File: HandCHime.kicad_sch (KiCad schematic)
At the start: 18 parts, among them J1 USB_C_Receptacle_USB2.0, J2 Pins, SW0 BOOT, SW1 Row 0, Col 0, SW2 Row 0, Col 1, U1 CH552T, U2 USBLC6-2P6

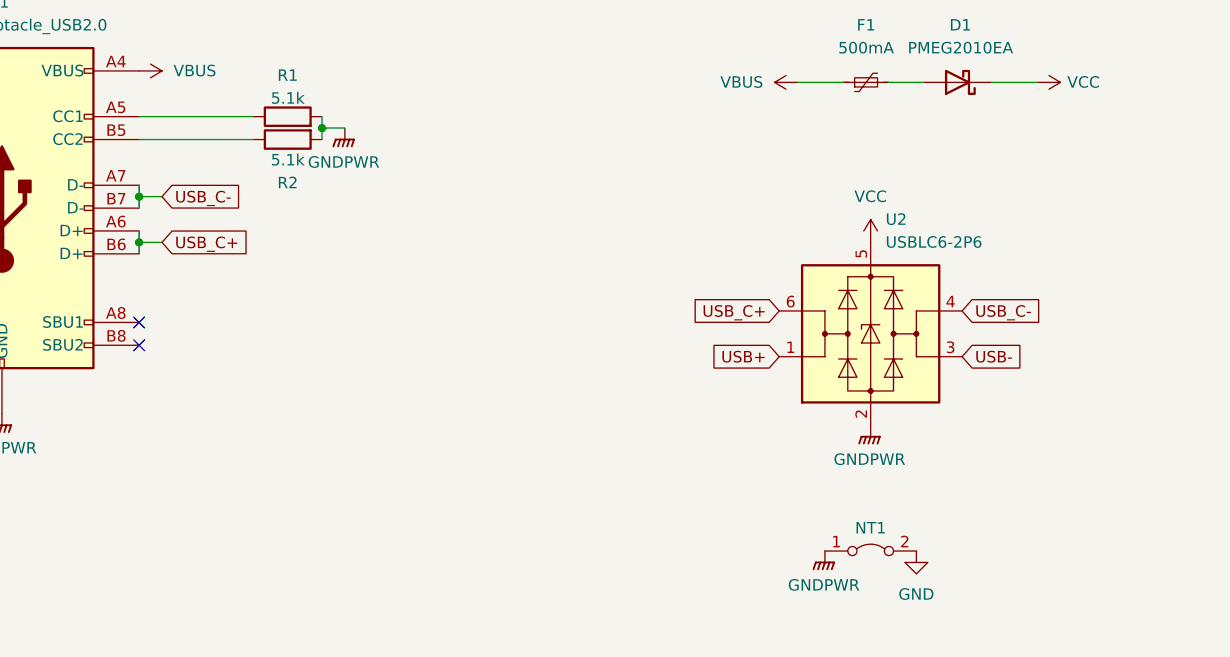
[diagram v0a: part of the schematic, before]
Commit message: Use smaller ESD chip
USBLC6-2SC6 → PRTR5V0U2X
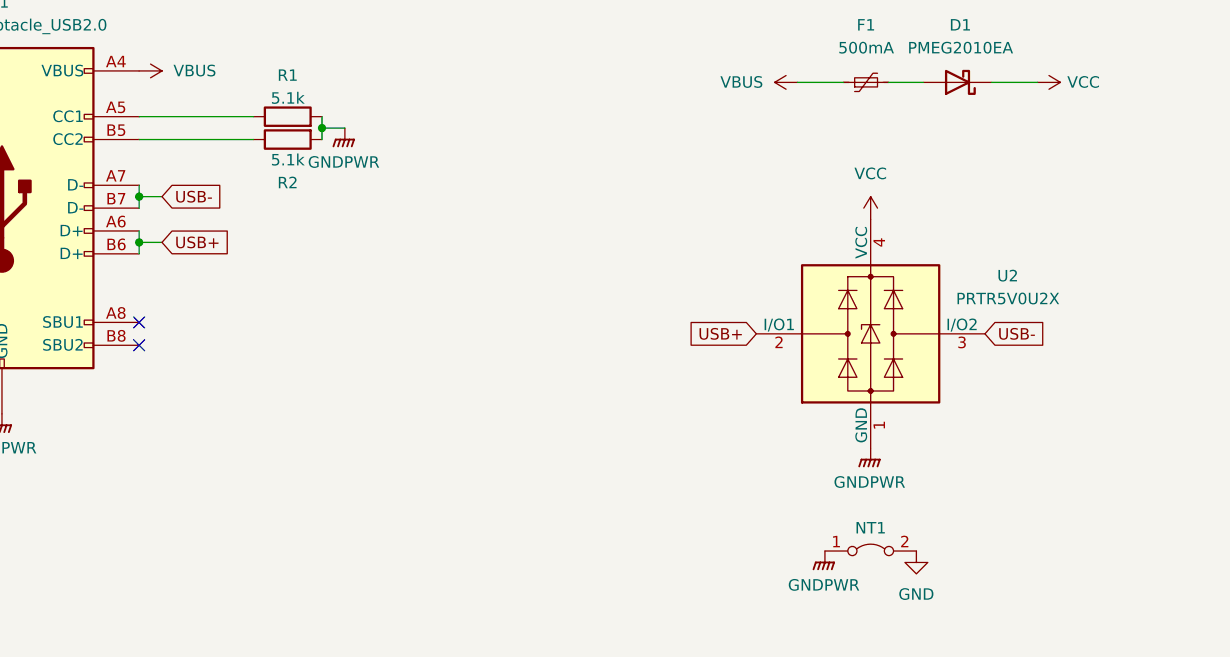
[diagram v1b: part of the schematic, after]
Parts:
- removed U2: USBLC6-2P6, Package_TO_SOT_SMD:SOT-23-6, symbol Power_Protection:USBLC6-2SC6
- added U2: PRTR5V0U2X, Package_TO_SOT_SMD:SOT-143, symbol Power_Protection:PRTR5V0U2X
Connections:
- net USB_C+ is gone; now on net USB+: J1.A6 (D+), J1.B6 (D+)
- net USB_C- is gone; now on net USB-: J1.A7 (D-), J1.B7 (D-)
- net GNDPWR: now also U2.1 (GND)
- net USB+: now also U2.2 (I/O1)
- net USB-: now also U2.3 (I/O2)
- net VCC: now also U2.4 (VCC)
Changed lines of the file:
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@@
 		)
 	)
-	(global_label "USB_C-"
-		(shape input)
-		(at 137.16 66.04 0)
-		(fields_autoplaced yes)
-		(effects
-			(font
-				(size 1.27 1.27)
-			)
-			(justify left)
-		)
-		(property "Intersheetrefs" "${INTERSHEET_REFS}"
-			(at 147.7652 66.04 0)
-			(effects
-				(font
-					(size 1.27 1.27)
-				)
-				(justify left)
-				(hide yes)
-			)
-		)
-	)
 	(global_label "P14"
 		(shape input)
@@
 		)
 	)
-	(global_label "USB_C+"
+	(global_label "USB+"
 		(shape input)
 		(at 48.26 58.42 0)
@@
 		)
 		(property "Intersheetrefs" "${INTERSHEET_REFS}"
-			(at 58.8652 58.42 0)
+			(at 56.6276 58.42 0)
 			(effects
 				(font
@@
 		)
 	)
-	(global_label "USB_C+"
-		(shape input)
-		(at 116.84 66.04 180)
-		(fields_autoplaced yes)
-		(effects
-			(font
-				(size 1.27 1.27)
-			)
-			(justify right)
-		)
-		(property "Intersheetrefs" "${INTERSHEET_REFS}"
-			(at 106.2348 66.04 0)
-			(effects
-				(font
-					(size 1.27 1.27)
-				)
-				(justify right)
-				(hide yes)
-			)
-		)
-	)
 	(global_label "USB-"
 		(shape input)
-		(at 137.16 71.12 0)
+		(at 139.7 68.58 0)
 		(fields_autoplaced yes)
 		(effects
@@
 		)
 		(property "Intersheetrefs" "${INTERSHEET_REFS}"
-			(at 145.5276 71.12 0)
+			(at 148.0676 68.58 0)
 			(effects
 				(font
@@
 		)
 	)
-	(global_label "USB_C-"
+	(global_label "USB-"
 		(shape input)
 		(at 48.26 53.34 0)
@@
 		)
 		(property "Intersheetrefs" "${INTERSHEET_REFS}"
-			(at 58.8652 53.34 0)
+			(at 56.6276 53.34 0)
 			(effects
 				(font
@@
 	(global_label "USB+"
 		(shape input)
-		(at 116.84 71.12 180)
+		(at 114.3 68.58 180)
 		(fields_autoplaced yes)
 		(effects
@@
 		)
 		(property "Intersheetrefs" "${INTERSHEET_REFS}"
-			(at 108.4724 71.12 0)
+			(at 105.9324 68.58 0)
 			(effects
 				(font
@@
 	)
 	(symbol
+		(lib_id "Power_Protection:PRTR5V0U2X")
+		(at 127 68.58 0)
+		(unit 1)
+		(exclude_from_sim no)
+		(in_bom yes)
+		(on_board yes)
+		(dnp no)
+		(fields_autoplaced yes)
+		(property "Reference" "U2"
+			(at 142.24 62.1598 0)
+			(effects
+				(font
+					(size 1.27 1.27)
+				)
+			)
+		)
+		(property "Value" "PRTR5V0U2X"
+			(at 142.24 64.6998 0)
+			(effects
+				(font
+					(size 1.27 1.27)
+				)
+			)
+		)
+		(property "Footprint" "Package_TO_SOT_SMD:SOT-143"
+			(at 128.524 68.58 0)
+			(effects
+				(font
+					(size 1.27 1.27)
+				)
+				(hide yes)
+			)
+		)
+		(property "Datasheet" "https://assets.nexperia.com/documents/data-sheet/PRTR5V0U2X.pdf"
+			(at 128.524 68.58 0)
+			(effects
+				(font
+					(size 1.27 1.27)
+				)
+				(hide yes)
+			)
+		)
+		(property "Description" "Ultra low capacitance double rail-to-rail ESD protection diode, SOT-143"
+			(at 127 68.58 0)
+			(effects
+				(font
+					(size 1.27 1.27)
+				)
+				(hide yes)
+			)
+		)
+		(property "LCSC" "C12333"
+			(at 127 68.58 0)
+			(effects
+				(font
+					(size 1.27 1.27)
+				)
+				(hide yes)
+			)
+		)
+		(property "DigiKey" "1727-3884-1-ND"
+			(at 127 68.58 0)
+			(effects
+				(font
+					(size 1.27 1.27)
+				)
+				(hide yes)
+			)
+		)
+		(pin "2"
+		)
+		(pin "3"
+		)
+		(pin "1"
+		)
+		(pin "4"
+		)
+		(instances
+			(project ""
+				(path "/34400e51-cf83-464a-b3ec-e9a28a972a27"
+					(reference "U2")
+					(unit 1)
+				)
+			)
+		)
+	)
+	(symbol
 		(lib_id "power:VCC")
-		(at 127 58.42 0)
+		(at 127 55.88 0)
 		(unit 1)
 		(exclude_from_sim no)
@@
 		(fields_autoplaced yes)
 		(property "Reference" "#PWR07"
-			(at 127 62.23 0)
+			(at 127 59.69 0)
 			(effects
 				(font
@@
 		)
 		(property "Value" "VCC"
-			(at 127 53.34 0)
+			(at 127 50.8 0)
 			(effects
 				(font
@@
 		)
 		(property "Footprint" ""
-			(at 127 58.42 0)
+			(at 127 55.88 0)
 			(effects
 				(font
@@
 		)
 		(property "Datasheet" ""
-			(at 127 58.42 0)
+			(at 127 55.88 0)
 			(effects
 				(font
@@
 		)
 		(property "Description" ""
-			(at 127 58.42 0)
+			(at 127 55.88 0)
 			(effects
 				(font
@@
 	)
 	(symbol
-		(lib_id "Power_Protection:USBLC6-2SC6")
-		(at 127 68.58 0)
-		(unit 1)
-		(exclude_from_sim no)
-		(in_bom yes)
-		(on_board yes)
-		(dnp no)
-		(fields_autoplaced yes)
-		(property "Reference" "U2"
-			(at 128.6511 55.88 0)
-			(effects
-				(font
-					(size 1.27 1.27)
-				)
-				(justify left)
-			)
-		)
-		(property "Value" "USBLC6-2P6"
-			(at 128.6511 58.42 0)
-			(effects
-				(font
-					(size 1.27 1.27)
-				)
-				(justify left)
-			)
-		)
-		(property "Footprint" "Package_TO_SOT_SMD:SOT-23-6"
-			(at 127 81.28 0)
-			(effects
-				(font
-					(size 1.27 1.27)
-				)
-				(hide yes)
-			)
-		)
-		(property "Datasheet" "https://www.st.com/resource/en/datasheet/usblc6-2.pdf"
-			(at 132.08 59.69 0)
-			(effects
-				(font
-					(size 1.27 1.27)
-				)
-				(hide yes)
-			)
-		)
-		(property "Description" ""
-			(at 127 68.58 0)
-			(effects
-				(font
-					(size 1.27 1.27)
-				)
-				(hide yes)
-			)
-		)
-		(property "LCSC" "C2827654"
-			(at 127 68.58 0)
-			(effects
-				(font
-					(size 1.27 1.27)
-				)
-				(hide yes)
-			)
-		)
-		(property "DigiKey" "497-5235"
-			(at 127 68.58 0)
-			(effects
-				(font
-					(size 1.27 1.27)
-				)
-				(hide yes)
-			)
-		)
-		(pin "2"
-		)
-		(pin "1"
-		)
-		(pin "3"
-		)
-		(pin "4"
-		)
-		(pin "5"
-		)
-		(pin "6"
-		)
-		(instances
-			(project "ISOCHet"
-				(path "/34400e51-cf83-464a-b3ec-e9a28a972a27"
-					(reference "U2")
-					(unit 1)
-				)
-			)
-		)
-	)
-	(symbol
 		(lib_id "power:GND")
 		(at 246.38 44.45 90)
@@
 	(symbol
 		(lib_id "power:GNDPWR")
-		(at 127 78.74 0)
+		(at 127 81.28 0)
 		(unit 1)
 		(exclude_from_sim no)
@@
 		(fields_autoplaced yes)
 		(property "Reference" "#PWR019"
-			(at 127 83.82 0)
+			(at 127 86.36 0)
 			(effects
 				(font
@@
 		)
 		(property "Value" "GNDPWR"
-			(at 126.873 82.55 0)
+			(at 126.873 85.09 0)
 			(effects
 				(font
@@
 		)
 		(property "Footprint" ""
-			(at 127 80.01 0)
+			(at 127 82.55 0)
 			(effects
 				(font
@@
 		)
 		(property "Datasheet" ""
-			(at 127 80.01 0)
+			(at 127 82.55 0)
 			(effects
 				(font
@@
 		)
 		(property "Description" "Power symbol creates a global label with name \"GNDPWR\" , global ground"
-			(at 127 78.74 0)
+			(at 127 81.28 0)
 			(effects
 				(font

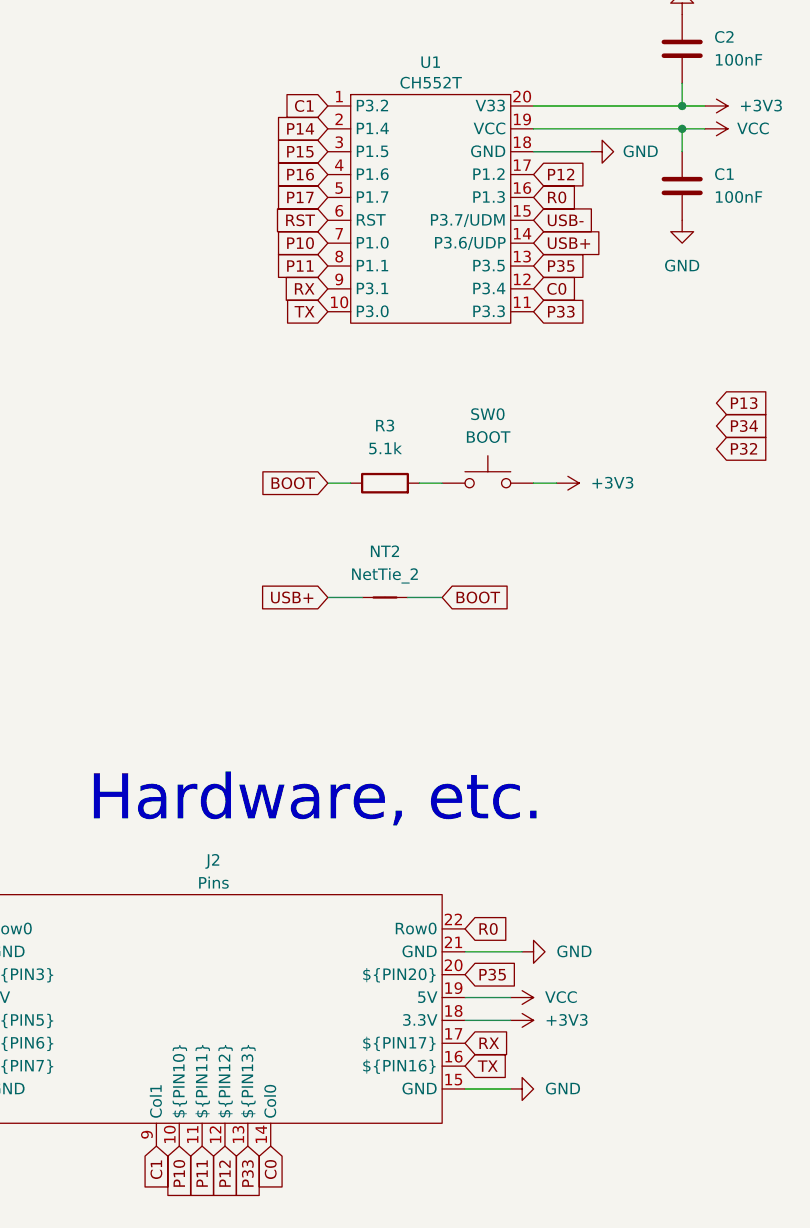
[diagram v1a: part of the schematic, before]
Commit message: Swap Row from P1.3 to P1.2 for better routing
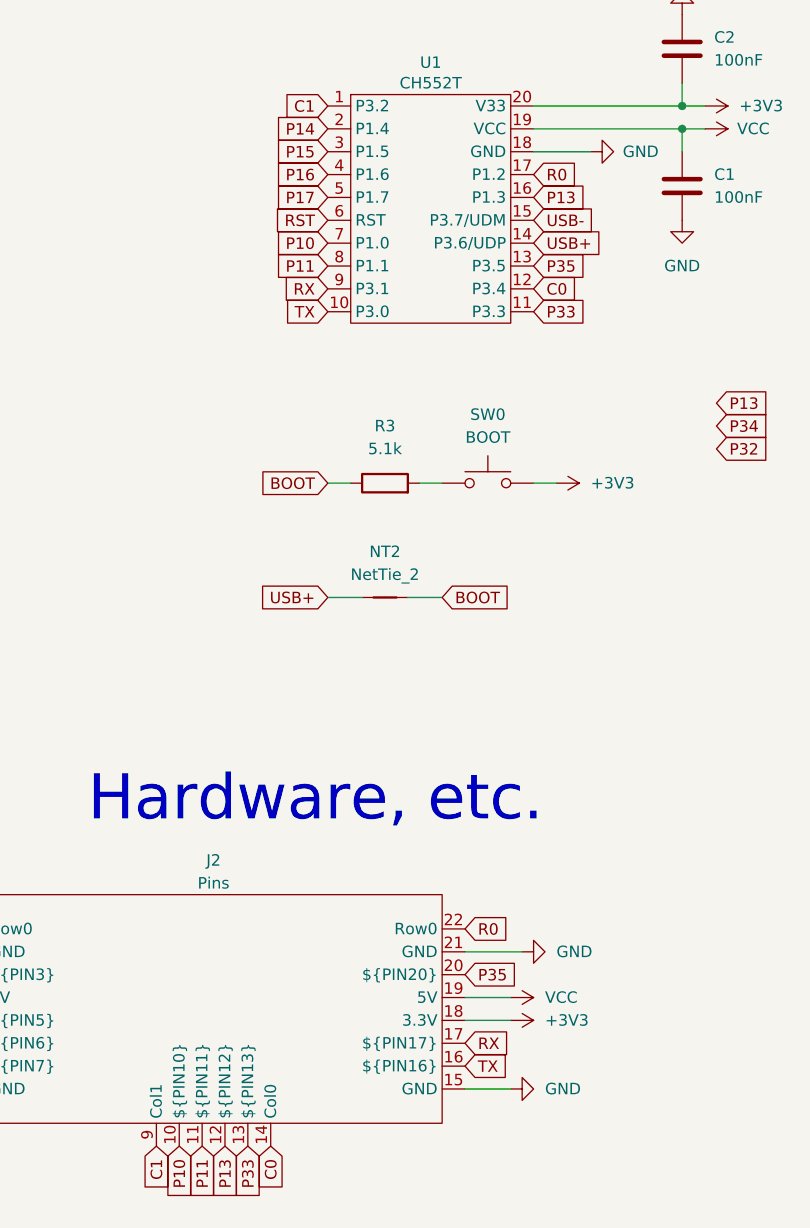
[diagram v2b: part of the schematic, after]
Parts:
- J2: PIN12 12 -> 13
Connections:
- net P13: now also J2.12 (${PIN12}), U1.16 (P1.3)
- net R0: now also U1.17 (P1.2); no longer U1.16 (P1.3)
- removed net P12: J2.12 (${PIN12}), U1.17 (P1.2)
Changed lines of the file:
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@@
 	(global_label "R0"
 		(shape input)
-		(at 240.03 49.53 0)
+		(at 240.03 46.99 0)
 		(fields_autoplaced yes)
 		(effects
@@
 		)
 		(property "Intersheetrefs" "${INTERSHEET_REFS}"
-			(at 245.4947 49.53 0)
+			(at 245.4947 46.99 0)
 			(effects
 				(font
@@
 		)
 	)
-	(global_label "P12"
+	(global_label "P13"
 		(shape input)
-		(at 240.03 46.99 0)
+		(at 240.03 49.53 0)
 		(fields_autoplaced yes)
 		(effects
@@
 		)
 		(property "Intersheetrefs" "${INTERSHEET_REFS}"
-			(at 246.7042 46.99 0)
+			(at 246.7042 49.53 0)
 			(effects
 				(font
@@
 		)
 	)
-	(global_label "P12"
+	(global_label "P13"
 		(shape input)
 		(at 205.74 154.94 270)
@@
 			)
 		)
-		(property "PIN12" "12"
+		(property "PIN12" "13"
 			(at 204.47 139.7 0)
 			(effects

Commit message: Minor tweaks
 * Round pads on boot button
 * Add back silkscreen for boot button
 * Improve pad size for Schottky diode (D1)
 * Tune VCC routing
 * Fix DRC errors on net ties
 * Fix board constraints to remove DRC errors on vias
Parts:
- D1: footprint Diode_SMD:D_SOD-323 -> Project Library:D_SOD-323
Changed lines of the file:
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@@
 			)
 		)
-		(property "Footprint" "Diode_SMD:D_SOD-323"
+		(property "Footprint" "Project Library:D_SOD-323"
 			(at 136.652 40.64 0)
 			(effects
